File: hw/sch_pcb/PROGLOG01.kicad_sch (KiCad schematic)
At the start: 66 parts, among them J1 JUMP_3X2, J10 HEADER_2x01_PARALLEL, J11 HEADER_2x01_PARALLEL, J13 HEADER_2x01_PARALLEL, J14 HEADER_2x01_PARALLEL, J15 HEADER_2x01_PARALLEL, J16 HEADER_2x01_PARALLEL, J17 HEADER_2x01_PARALLEL, J18 HEADER_2x01_PARALLEL, J19 HEADER_2x01_PARALLEL, J2 HEADER_2x01, J20 HEADER_2x01_PARALLEL, J21 HEADER_2x01_PARALLEL, J22 HEADER_2x01_PARALLEL, J23 HEADER_2x01_PARALLEL, J24 HEADER_2x01_PARALLEL, J25 HEADER_2x01_PARALLEL, J26 SATA, J27 HEADER_2x01_PARALLEL, J28 HEADER_2x01_PARALLEL, J29 HEADER_2x01_PARALLEL, J3 HEADER_2x02_PARALLEL, J30 HEADER_2x01_PARALLEL, J31 HEADER_2x01_PARALLEL, J32 HEADER_2x01_PARALLEL, J33 HEADER_2x01_PARALLEL, J34 HEADER_2x01_PARALLEL, J4 HEADER_2x04, J5 HEADER_2x01_PARALLEL, J6 HEADER_2x01_PARALLEL, J7 HEADER_2x01_PARALLEL, J8 HEADER_2x01_PARALLEL, J9 HEADER_2x01_PARALLEL, M1 HOLE, M2 HOLE, M3 HOLE, M4 HOLE, SW1 SW_Push, U1 TPS22919DCK, U2 MIC5504-1.2YM5, U3 AT25SF081-SSH, U4 ICE40UP5K-SG48ITR, X1 ISM92-3351AH24.00

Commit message: Update project and documentation.
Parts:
- U4: value ICE40UP5K-SG48ITR -> ICE40UP5K-SG48I
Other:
- note removed: "BLUE"
- note removed: "YELLOW"
- title: PROGLOG01A -> PROGLOG01B
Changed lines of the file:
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@@
   (paper "A4")
   (title_block
-    (title "PROGLOG01A")
+    (title "PROGLOG01B")
     (date "2022-02-13")
     (company "Mlab www.mlab.cz")
@@
     (effects (font (size 1.524 1.524)) (justify left bottom))
   )
-  (text "BLUE" (at 265.43 77.47 90)
-    (effects (font (size 1.524 1.524)) (justify left bottom))
-  )
   (text "MOUNTING HOLES" (at 17.78 27.94 0)
     (effects (font (size 1.524 1.524)) (justify left bottom))
@@
     (effects (font (size 1.524 1.524)) (justify left bottom))
   )
-  (text "YELLOW" (at 245.11 77.47 90)
-    (effects (font (size 1.524 1.524)) (justify left bottom))
-  )
   (text "POWER INPUT" (at 34.29 57.15 180)
     (effects (font (size 1.524 1.524)) (justify right bottom))
@@
       (effects (font (size 1.27 1.27)) (justify left))
     )
-    (property "Value" "ICE40UP5K-SG48ITR" (id 1) (at 161.29 86.36 90)
+    (property "Value" "ICE40UP5K-SG48I" (id 1) (at 161.29 86.36 90)
       (effects (font (size 1.27 1.27)) (justify left))
     )
@@
       (effects (font (size 1.27 1.27)) hide)
     )
-    (property "Datasheet" "file:///home/kaklik/Downloads/FPGA-DS-02008-1-9-iCE40-UltraPlus-Family-Data-Sheet.pdf" (id 3) (at 181.61 36.83 0)
+    (property "Datasheet" "https://www.latticesemi.com/-/media/LatticeSemi/Documents/DataSheets/iCE/iCE40%20UltraPlus%20Family%20Data%20Sheet.pdf?document_id=51968" (id 3) (at 181.61 36.83 0)
       (effects (font (size 1.27 1.27)) hide)
     )
@@
     (in_bom yes) (on_board yes)
     (property "Reference" "U4" (id 0) (at 217.17 155.5496 0))
-    (property "Value" "ICE40UP5K-SG48ITR" (id 1) (at 217.17 157.861 0))
+    (property "Value" "ICE40UP5K-SG48I" (id 1) (at 217.17 157.861 0))
     (property "Footprint" "Package_DFN_QFN:QFN-48-1EP_7x7mm_P0.5mm_EP5.6x5.6mm" (id 2) (at 217.17 162.56 0)
       (effects (font (size 1.27 1.27)) hide)
     )
-    (property "Datasheet" "file:///home/kaklik/Downloads/FPGA-DS-02008-1-9-iCE40-UltraPlus-Family-Data-Sheet.pdf" (id 3) (at 207.01 102.87 0)
+    (property "Datasheet" "https://www.latticesemi.com/-/media/LatticeSemi/Documents/DataSheets/iCE/iCE40%20UltraPlus%20Family%20Data%20Sheet.pdf?document_id=51968" (id 3) (at 207.01 102.87 0)
       (effects (font (size 1.27 1.27)) hide)
     )
@@
       (effects (font (size 1.27 1.27)) (justify left))
     )
-    (property "Value" "ICE40UP5K-SG48ITR" (id 1) (at 232.41 151.13 90)
+    (property "Value" "ICE40UP5K-SG48I" (id 1) (at 232.41 151.13 90)
       (effects (font (size 1.27 1.27)) (justify left))
     )
@@
       (effects (font (size 1.27 1.27)) hide)
     )
-    (property "Datasheet" "file:///home/kaklik/Downloads/FPGA-DS-02008-1-9-iCE40-UltraPlus-Family-Data-Sheet.pdf" (id 3) (at 252.73 111.76 0)
+    (property "Datasheet" "https://www.latticesemi.com/-/media/LatticeSemi/Documents/DataSheets/iCE/iCE40%20UltraPlus%20Family%20Data%20Sheet.pdf?document_id=51968" (id 3) (at 252.73 111.76 0)
       (effects (font (size 1.27 1.27)) hide)
     )
@@
     (in_bom yes) (on_board yes)
     (property "Reference" "U4" (id 0) (at 119.38 176.53 90))
-    (property "Value" "ICE40UP5K-SG48ITR" (id 1) (at 115.57 163.83 90))
+    (property "Value" "ICE40UP5K-SG48I" (id 1) (at 115.57 163.83 90))
     (property "Footprint" "Package_DFN_QFN:QFN-48-1EP_7x7mm_P0.5mm_EP5.6x5.6mm" (id 2) (at 149.86 170.18 0)
       (effects (font (size 1.27 1.27)) hide)
     )
-    (property "Datasheet" "file:///home/kaklik/Downloads/FPGA-DS-02008-1-9-iCE40-UltraPlus-Family-Data-Sheet.pdf" (id 3) (at 90.17 160.02 0)
+    (property "Datasheet" "https://www.latticesemi.com/-/media/LatticeSemi/Documents/DataSheets/iCE/iCE40%20UltraPlus%20Family%20Data%20Sheet.pdf?document_id=51968" (id 3) (at 90.17 160.02 0)
       (effects (font (size 1.27 1.27)) hide)
     )
@@
       (effects (font (size 1.27 1.27)) (justify right))
     )
-    (property "Value" "BLUE" (id 1) (at 260.35 73.66 0)
+    (property "Value" "BLUE" (id 1) (at 264.16 69.85 0)
       (effects (font (size 1.27 1.27)) (justify right))
     )
@@
       (effects (font (size 1.27 1.27)) (justify right))
     )
-    (property "Value" "YELLOW" (id 1) (at 251.46 72.39 0)
+    (property "Value" "YELLOW" (id 1) (at 243.84 69.85 0)
       (effects (font (size 1.27 1.27)) (justify right))
     )
@@
     )
     (path "/00000000-0000-0000-0000-00005d8c3cd5"
-      (reference "U4") (unit 1) (value "ICE40UP5K-SG48ITR") (footprint "Package_DFN_QFN:QFN-48-1EP_7x7mm_P0.5mm_EP5.6x5.6mm")
+      (reference "U4") (unit 1) (value "ICE40UP5K-SG48I") (footprint "Package_DFN_QFN:QFN-48-1EP_7x7mm_P0.5mm_EP5.6x5.6mm")
     )
     (path "/00000000-0000-0000-0000-00005d8c3d71"
-      (reference "U4") (unit 2) (value "ICE40UP5K-SG48ITR") (footprint "Package_DFN_QFN:QFN-48-1EP_7x7mm_P0.5mm_EP5.6x5.6mm")
+      (reference "U4") (unit 2) (value "ICE40UP5K-SG48I") (footprint "Package_DFN_QFN:QFN-48-1EP_7x7mm_P0.5mm_EP5.6x5.6mm")
     )
     (path "/00000000-0000-0000-0000-00005d8c3df4"
-      (reference "U4") (unit 3) (value "ICE40UP5K-SG48ITR") (footprint "Package_DFN_QFN:QFN-48-1EP_7x7mm_P0.5mm_EP5.6x5.6mm")
+      (reference "U4") (unit 3) (value "ICE40UP5K-SG48I") (footprint "Package_DFN_QFN:QFN-48-1EP_7x7mm_P0.5mm_EP5.6x5.6mm")
     )
     (path "/00000000-0000-0000-0000-00005d8c3e7c"
-      (reference "U4") (unit 4) (value "ICE40UP5K-SG48ITR") (footprint "Package_DFN_QFN:QFN-48-1EP_7x7mm_P0.5mm_EP5.6x5.6mm")
+      (reference "U4") (unit 4) (value "ICE40UP5K-SG48I") (footprint "Package_DFN_QFN:QFN-48-1EP_7x7mm_P0.5mm_EP5.6x5.6mm")
     )
     (path "/00000000-0000-0000-0000-00005da56edd"

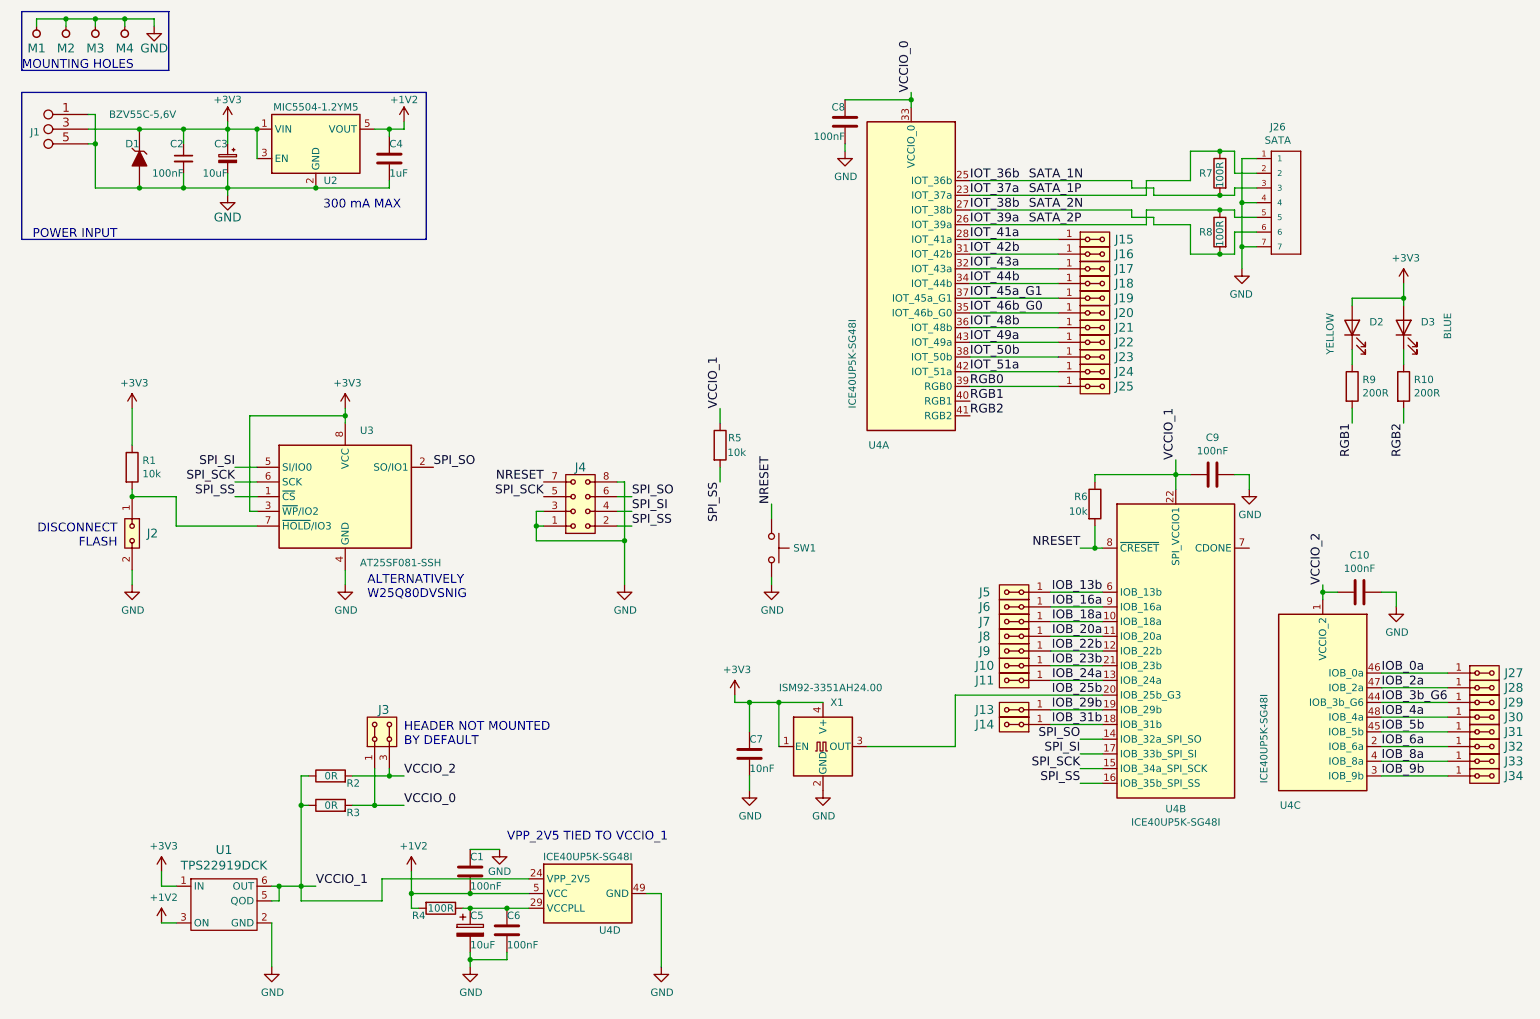
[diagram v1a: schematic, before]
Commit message: Repair #1 in schematics.
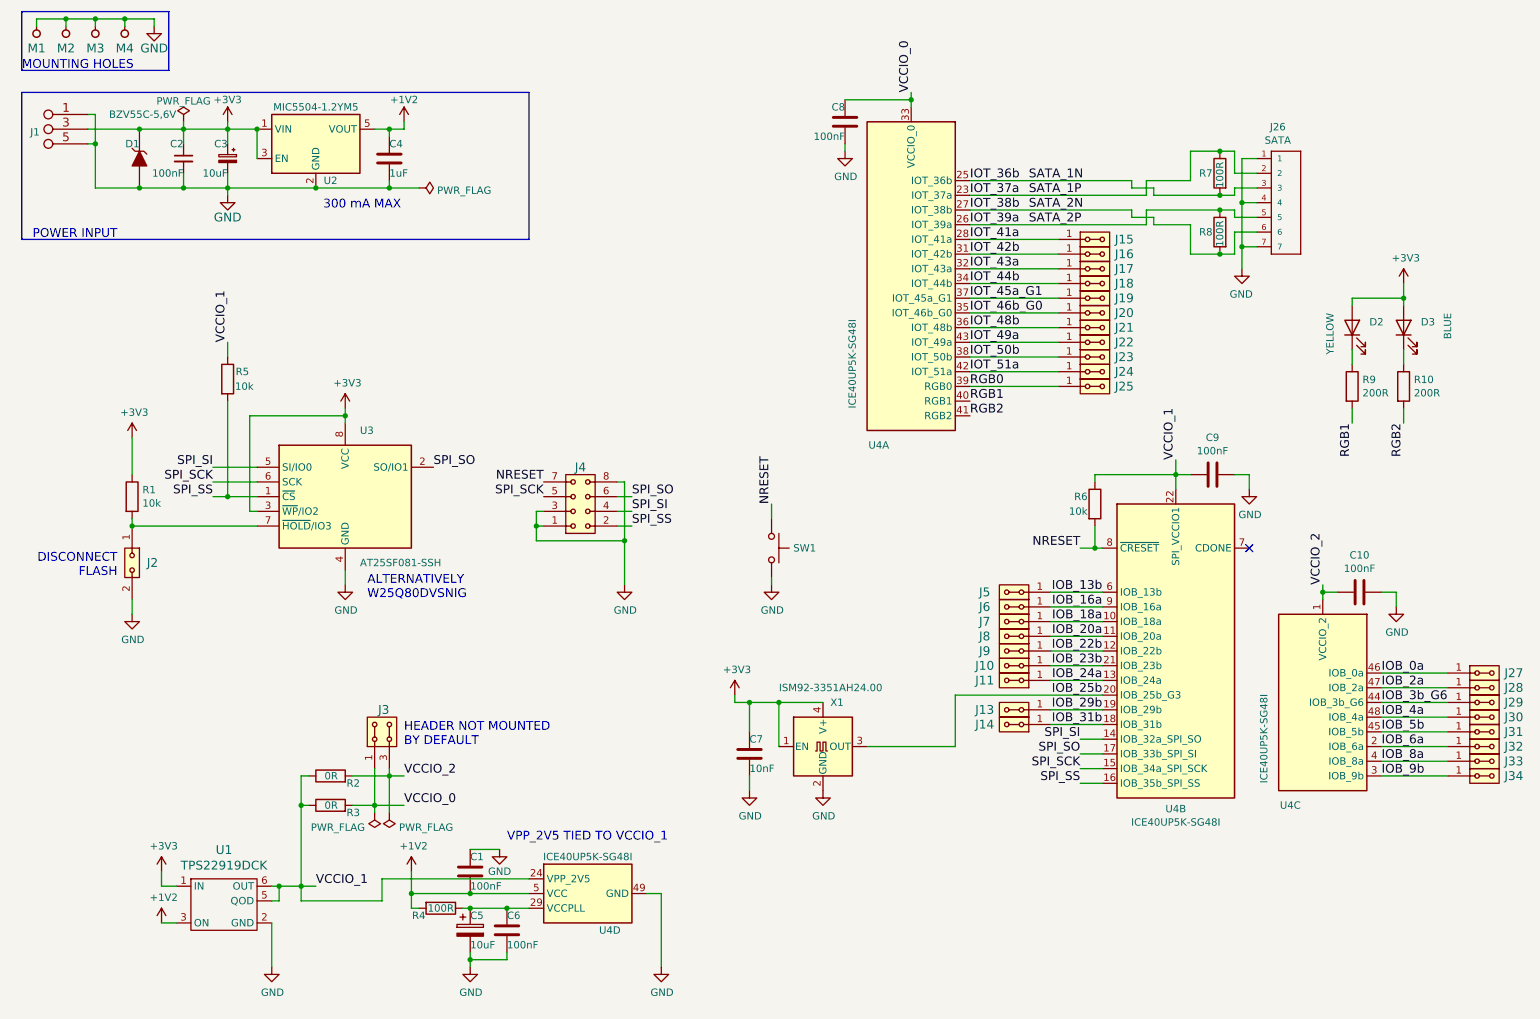
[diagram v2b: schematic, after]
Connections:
- net SPI_SI: now also U4.14 (IOB_32a_SPI_SO); no longer U4.17 (IOB_33b_SPI_SI)
- net SPI_SO: now also U4.17 (IOB_33b_SPI_SI); no longer U4.14 (IOB_32a_SPI_SO)
- no-connect marks 0 -> 1
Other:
- moved on the sheet: J2, R1, R5

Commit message: Update footprints from library. Improve bottom silkscreen.
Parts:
- C1, C10, C2, C3, C4, C5, C6, C7, C8, C9: footprint Mlab_R:SMD-0805 -> Capacitor_SMD:C_0805_2012Metric
- R1, R10, R2, R3, R4, R5, R6, R7, R8, R9: footprint Mlab_R:SMD-0805 -> Resistor_SMD:R_0805_2012Metric
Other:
- moved on the sheet: C1, C5, C6

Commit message: Fix wrong UST_ID assigned.
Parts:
- C4: UST_ID 5c70984812875079b91f8bc2 -> 5c70984712875079b91f8b50
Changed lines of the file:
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@@
       (effects (font (size 1.27 1.27)) hide)
     )
-    (property "UST_ID" "5c70984812875079b91f8bc2" (id 4) (at 81.28 43.18 0)
+    (property "UST_ID" "5c70984712875079b91f8b50" (id 4) (at 81.28 43.18 0)
       (effects (font (size 1.27 1.27)) hide)
     )

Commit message: Update schematics symbols.
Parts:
- C3: symbol Device:CP_Small -> Device:C_Polarized
- C5: symbol Device:CP -> Device:C_Polarized
- J26: footprint Mlab_CON:SATA-7_THT_VERT_2 -> MOLEX_67491-1030
- U2: footprint Package_TO_SOT_SMD:SOT-23-5_HandSoldering -> Package_TO_SOT_SMD:SOT-23-5
- U3: footprint Mlab_IO:SOIC-8_3.9x4.9mm_Pitch1.27mm -> Package_SO:SOIC-8_3.9x4.9mm_P1.27mm
- U4: symbol PROGLOG01A-rescue:ICE40UP5K-SG48ITR-FPGA_Lattice -> FPGA_Lattice:ICE40UP5K-SG48ITR
- X1: footprint Mlab_XTAL:ISM92 -> Oscillator:Oscillator_SMD_EuroQuartz_XO91-4Pin_7.0x5.0mm
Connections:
- net +3V3: no longer C3.1
- net GND: no longer C3.2
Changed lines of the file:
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@@
       (effects (font (size 1.524 1.524)) hide)
     )
-    (property "Datasheet" "" (id 3) (at 45.72 43.18 0)
+    (property "Datasheet" "~" (id 3) (at 45.72 43.18 0)
       (effects (font (size 1.524 1.524)))
     )
@@
     (pin "2")
   )
-  (symbol (lib_id "Device:CP_Small") (at 53.34 43.18 0) (mirror y) (unit 1)
+  (symbol (lib_id "Device:C_Polarized") (at 53.34 43.18 0) (mirror y) (unit 1)
     (in_bom yes) (on_board yes)
     (property "Reference" "C3" (id 0) (at 53.34 40.64 0)
@@
       (effects (font (size 1.27 1.27)) (justify left))
     )
-    (property "Footprint" "Capacitor_SMD:C_0805_2012Metric" (id 2) (at 53.34 43.18 0)
-      (effects (font (size 1.524 1.524)) hide)
-    )
-    (property "Datasheet" "" (id 3) (at 53.34 43.18 0)
-      (effects (font (size 1.524 1.524)))
+    (property "Footprint" "Capacitor_SMD:C_0805_2012Metric" (id 2) (at 52.3748 46.99 0)
+      (effects (font (size 1.27 1.27)) hide)
+    )
+    (property "Datasheet" "~" (id 3) (at 53.34 43.18 0)
+      (effects (font (size 1.27 1.27)) hide)
     )
     (property "UST_ID" "5c70984812875079b91f8bbd" (id 4) (at 53.34 43.18 0)
@@
     (pin "2")
   )
-  (symbol (lib_id "PROGLOG01A-rescue:ICE40UP5K-SG48ITR-FPGA_Lattice") (at 171.45 62.23 0) (mirror y) (unit 1)
+  (symbol (lib_id "FPGA_Lattice:ICE40UP5K-SG48ITR") (at 171.45 62.23 0) (mirror y) (unit 1)
     (in_bom yes) (on_board yes)
     (property "Reference" "U4" (id 0) (at 167.64 92.71 0)
@@
       (effects (font (size 1.27 1.27)) hide)
     )
-    (property "Datasheet" "https://www.latticesemi.com/-/media/LatticeSemi/Documents/DataSheets/iCE/iCE40%20UltraPlus%20Family%20Data%20Sheet.pdf?document_id=51968" (id 3) (at 181.61 36.83 0)
+    (property "Datasheet" "http://www.latticesemi.com/Products/FPGAandCPLD/iCE40Ultra" (id 3) (at 181.61 36.83 0)
       (effects (font (size 1.27 1.27)) hide)
     )
@@
     (pin "5")
   )
-  (symbol (lib_id "PROGLOG01A-rescue:ICE40UP5K-SG48ITR-FPGA_Lattice") (at 217.17 128.27 0) (unit 2)
+  (symbol (lib_id "FPGA_Lattice:ICE40UP5K-SG48ITR") (at 217.17 128.27 0) (unit 2)
     (in_bom yes) (on_board yes)
     (property "Reference" "U4" (id 0) (at 217.17 155.5496 0))
@@
       (effects (font (size 1.27 1.27)) hide)
     )
-    (property "Datasheet" "https://www.latticesemi.com/-/media/LatticeSemi/Documents/DataSheets/iCE/iCE40%20UltraPlus%20Family%20Data%20Sheet.pdf?document_id=51968" (id 3) (at 207.01 102.87 0)
+    (property "Datasheet" "http://www.latticesemi.com/Products/FPGAandCPLD/iCE40Ultra" (id 3) (at 207.01 102.87 0)
       (effects (font (size 1.27 1.27)) hide)
     )
@@
     (pin "5")
   )
-  (symbol (lib_id "PROGLOG01A-rescue:ICE40UP5K-SG48ITR-FPGA_Lattice") (at 242.57 137.16 0) (mirror y) (unit 3)
+  (symbol (lib_id "FPGA_Lattice:ICE40UP5K-SG48ITR") (at 242.57 137.16 0) (mirror y) (unit 3)
     (in_bom yes) (on_board yes)
     (property "Reference" "U4" (id 0) (at 238.76 154.94 0)
@@
       (effects (font (size 1.27 1.27)) hide)
     )
-    (property "Datasheet" "https://www.latticesemi.com/-/media/LatticeSemi/Documents/DataSheets/iCE/iCE40%20UltraPlus%20Family%20Data%20Sheet.pdf?document_id=51968" (id 3) (at 252.73 111.76 0)
+    (property "Datasheet" "http://www.latticesemi.com/Products/FPGAandCPLD/iCE40Ultra" (id 3) (at 252.73 111.76 0)
       (effects (font (size 1.27 1.27)) hide)
     )
@@
     (pin "5")
   )
-  (symbol (lib_id "PROGLOG01A-rescue:ICE40UP5K-SG48ITR-FPGA_Lattice") (at 115.57 170.18 90) (mirror x) (unit 4)
+  (symbol (lib_id "FPGA_Lattice:ICE40UP5K-SG48ITR") (at 115.57 170.18 90) (mirror x) (unit 4)
     (in_bom yes) (on_board yes)
     (property "Reference" "U4" (id 0) (at 119.38 176.53 90))
@@
       (effects (font (size 1.27 1.27)) hide)
     )
-    (property "Datasheet" "https://www.latticesemi.com/-/media/LatticeSemi/Documents/DataSheets/iCE/iCE40%20UltraPlus%20Family%20Data%20Sheet.pdf?document_id=51968" (id 3) (at 90.17 160.02 0)
+    (property "Datasheet" "http://www.latticesemi.com/Products/FPGAandCPLD/iCE40Ultra" (id 3) (at 90.17 160.02 0)
       (effects (font (size 1.27 1.27)) hide)
     )
@@
       (effects (font (size 1.27 1.27)) (justify left))
     )
-    (property "Footprint" "Mlab_XTAL:ISM92" (id 2) (at 173.99 153.67 0)
+    (property "Footprint" "Oscillator:Oscillator_SMD_EuroQuartz_XO91-4Pin_7.0x5.0mm" (id 2) (at 173.99 153.67 0)
       (effects (font (size 1.27 1.27)) hide)
     )
@@
     (property "Reference" "U2" (id 0) (at 71.12 46.99 0))
     (property "Value" "MIC5504-1.2YM5" (id 1) (at 68.58 34.29 0))
-    (property "Footprint" "Package_TO_SOT_SMD:SOT-23-5_HandSoldering" (id 2) (at 68.58 50.8 0)
+    (property "Footprint" "Package_TO_SOT_SMD:SOT-23-5" (id 2) (at 68.58 50.8 0)
       (effects (font (size 1.27 1.27)) hide)
     )
@@
     (pin "2")
   )
-  (symbol (lib_id "Device:CP") (at 95.25 177.8 0) (unit 1)
+  (symbol (lib_id "Device:C_Polarized") (at 95.25 177.8 0) (unit 1)
     (in_bom yes) (on_board yes)
     (property "Reference" "C5" (id 0) (at 95.25 175.26 0)
@@
     (property "Reference" "J26" (id 0) (at 234.7976 37.719 0))
     (property "Value" "SATA" (id 1) (at 234.7976 40.0304 0))
-    (property "Footprint" "Mlab_CON:SATA-7_THT_VERT_2" (id 2) (at 236.22 46.99 0)
+    (property "Footprint" "MOLEX_67491-1030" (id 2) (at 236.22 46.99 0)
       (effects (font (size 1.27 1.27)) hide)
     )
@@
       (effects (font (size 1.27 1.27)) (justify left))
     )
-    (property "Footprint" "Mlab_IO:SOIC-8_3.9x4.9mm_Pitch1.27mm" (id 2) (at 73.66 116.84 0)
-      (effects (font (size 1.27 1.27)) hide)
-    )
-    (property "Datasheet" "https://www.renesas.com/us/en/document/dst/at25sf081-datasheet" (id 3) (at 73.66 101.6 0)
+    (property "Footprint" "Package_SO:SOIC-8_3.9x4.9mm_P1.27mm" (id 2) (at 73.66 116.84 0)
+      (effects (font (size 1.27 1.27)) hide)
+    )
+    (property "Datasheet" "https://www.adestotech.com/wp-content/uploads/DS-AT25SF081_045.pdf" (id 3) (at 73.66 101.6 0)
       (effects (font (size 1.27 1.27)) hide)
     )
@@
     )
     (path "/00000000-0000-0000-0000-00005dc4b4c2"
-      (reference "J26") (unit 1) (value "SATA") (footprint "Mlab_CON:SATA-7_THT_VERT_2")
+      (reference "J26") (unit 1) (value "SATA") (footprint "MOLEX_67491-1030")
     )
     (path "/00000000-0000-0000-0000-00005db17a62"
@@
     )
     (path "/00000000-0000-0000-0000-00005db46f40"
-      (reference "U2") (unit 1) (value "MIC5504-1.2YM5") (footprint "Package_TO_SOT_SMD:SOT-23-5_HandSoldering")
+      (reference "U2") (unit 1) (value "MIC5504-1.2YM5") (footprint "Package_TO_SOT_SMD:SOT-23-5")
     )
     (path "/00000000-0000-0000-0000-00005e086457"
-      (reference "U3") (unit 1) (value "AT25SF081-SSH") (footprint "Mlab_IO:SOIC-8_3.9x4.9mm_Pitch1.27mm")
+      (reference "U3") (unit 1) (value "AT25SF081-SSH") (footprint "Package_SO:SOIC-8_3.9x4.9mm_P1.27mm")
     )
     (path "/00000000-0000-0000-0000-00005d8c3cd5"
@@
     )
     (path "/00000000-0000-0000-0000-00005da56edd"
-      (reference "X1") (unit 1) (value "ISM92-3351AH24.00") (footprint "Mlab_XTAL:ISM92")
-    )
-  )
+      (reference "X1") (unit 1) (value "ISM92-3351AH24.00") (footprint "Oscillator:Oscillator_SMD_EuroQuartz_XO91-4Pin_7.0x5.0mm")
+    )
+  )
